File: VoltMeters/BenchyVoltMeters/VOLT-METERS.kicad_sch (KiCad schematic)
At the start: 71 parts, among them U1 INA826AIDRGR, U11 APX321

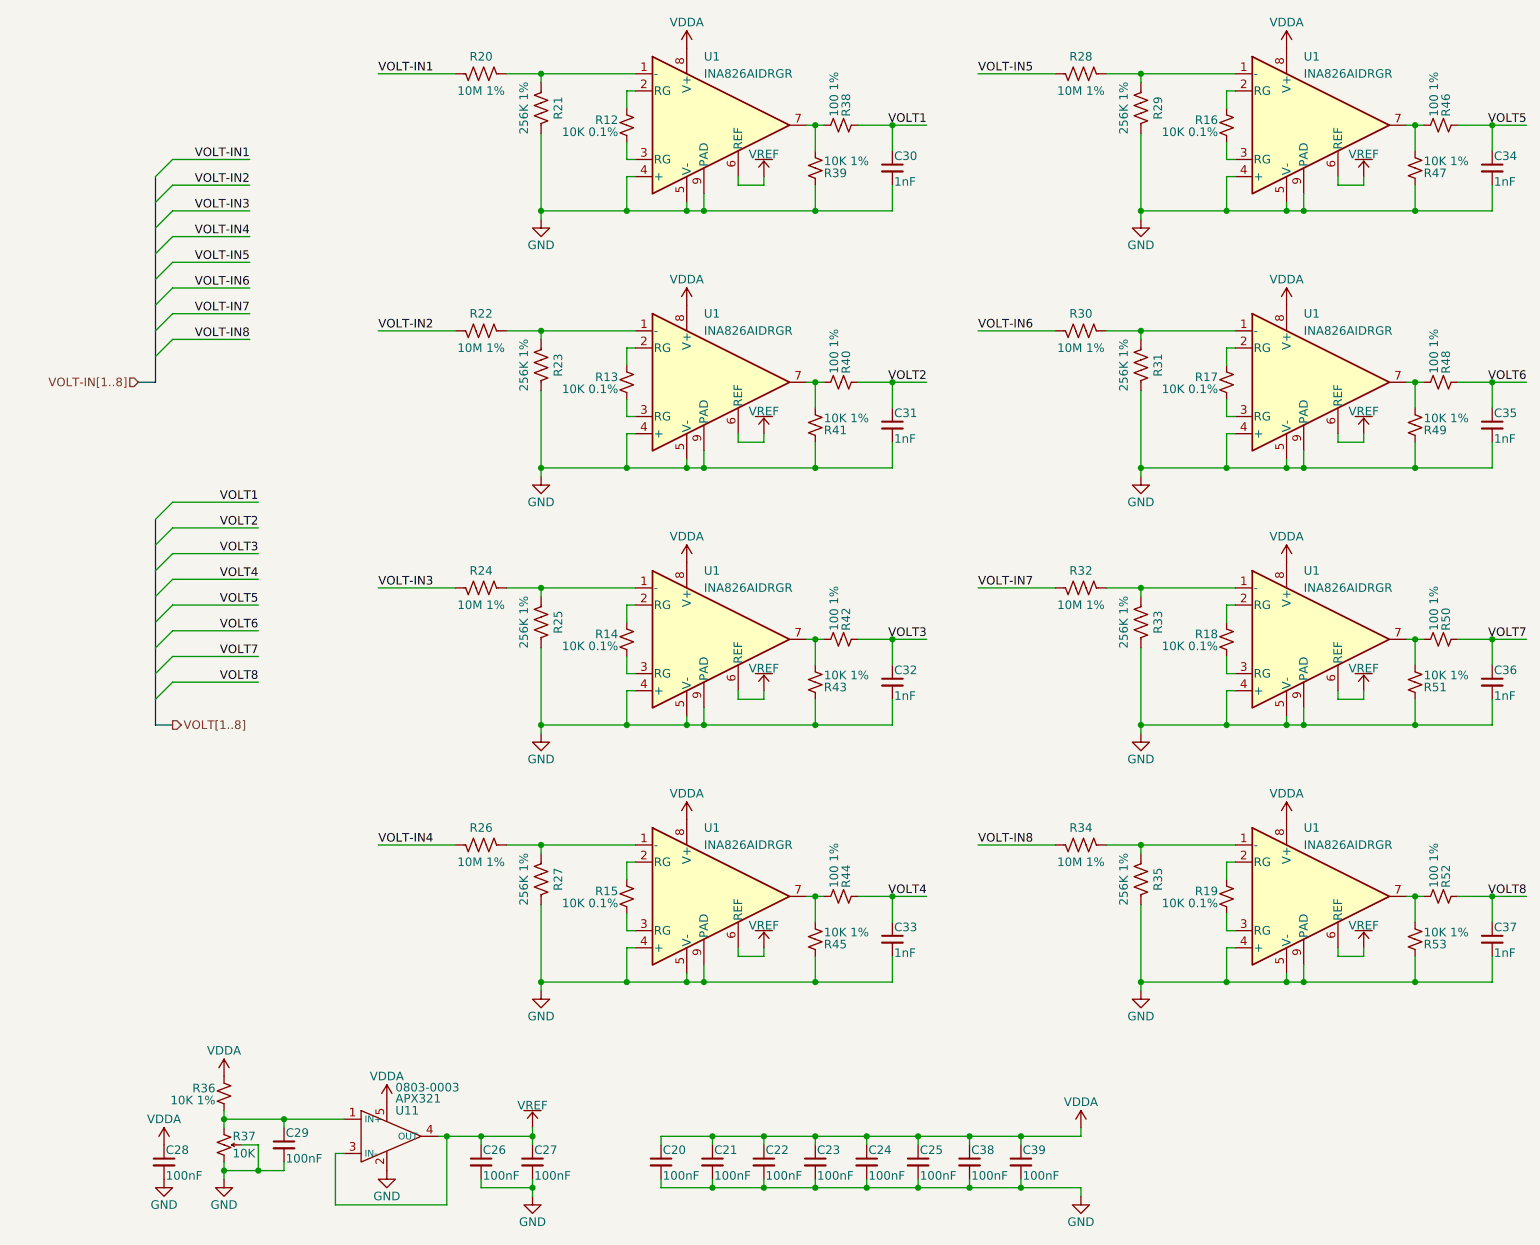
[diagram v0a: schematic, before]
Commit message: Add voltmeter PCB
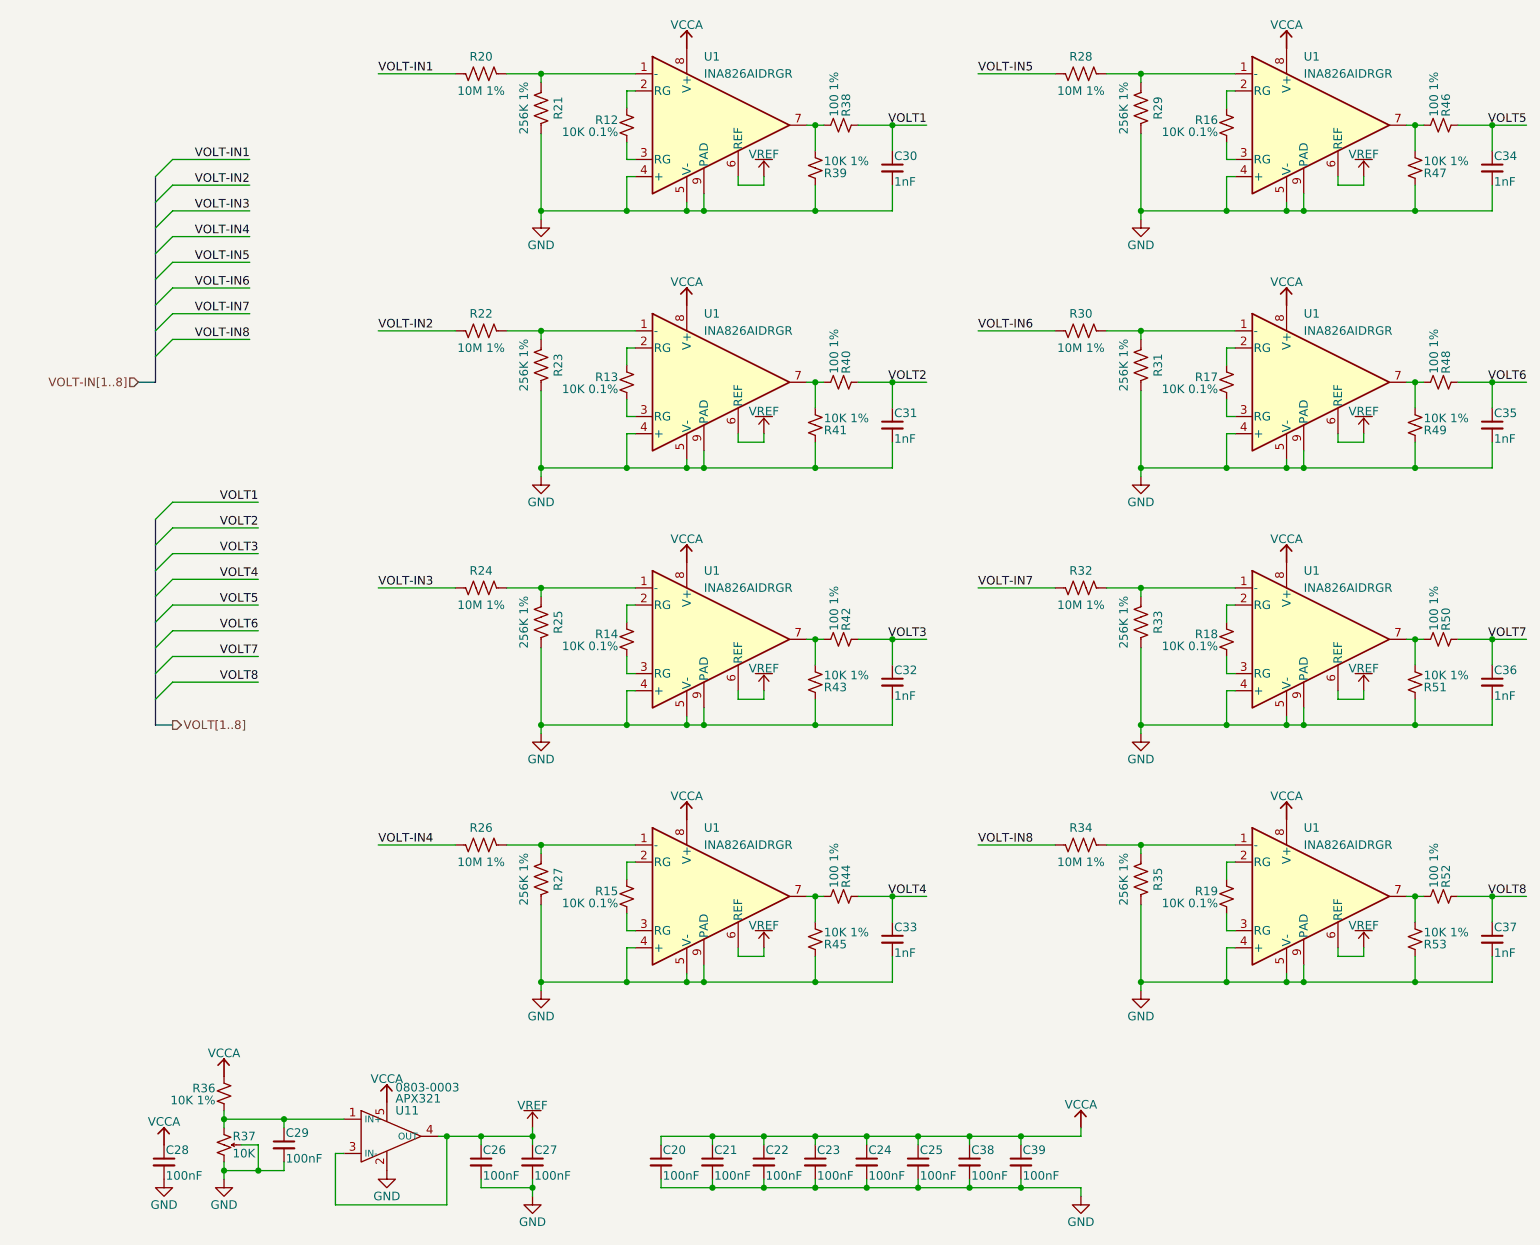
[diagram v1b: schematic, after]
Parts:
- C20, C21, C22, C23, C24, C25, C26, C27, C28, C29, C30, C31, C32, C33, C34, C35, C36, C37, C38, C39: footprint Resistor_SMD:R_0402_1005Metric -> Capacitor_SMD:C_0402_1005Metric
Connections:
- net VDDA renamed VCCA
